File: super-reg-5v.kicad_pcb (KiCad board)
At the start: 2 copper layers, 80 x 34.3 mm, 40 parts, among them Q1 2SA1015, Q2 D44H11, U1 LM317T, U2 AD825, X1 AC_IN, X2 DC_OUT

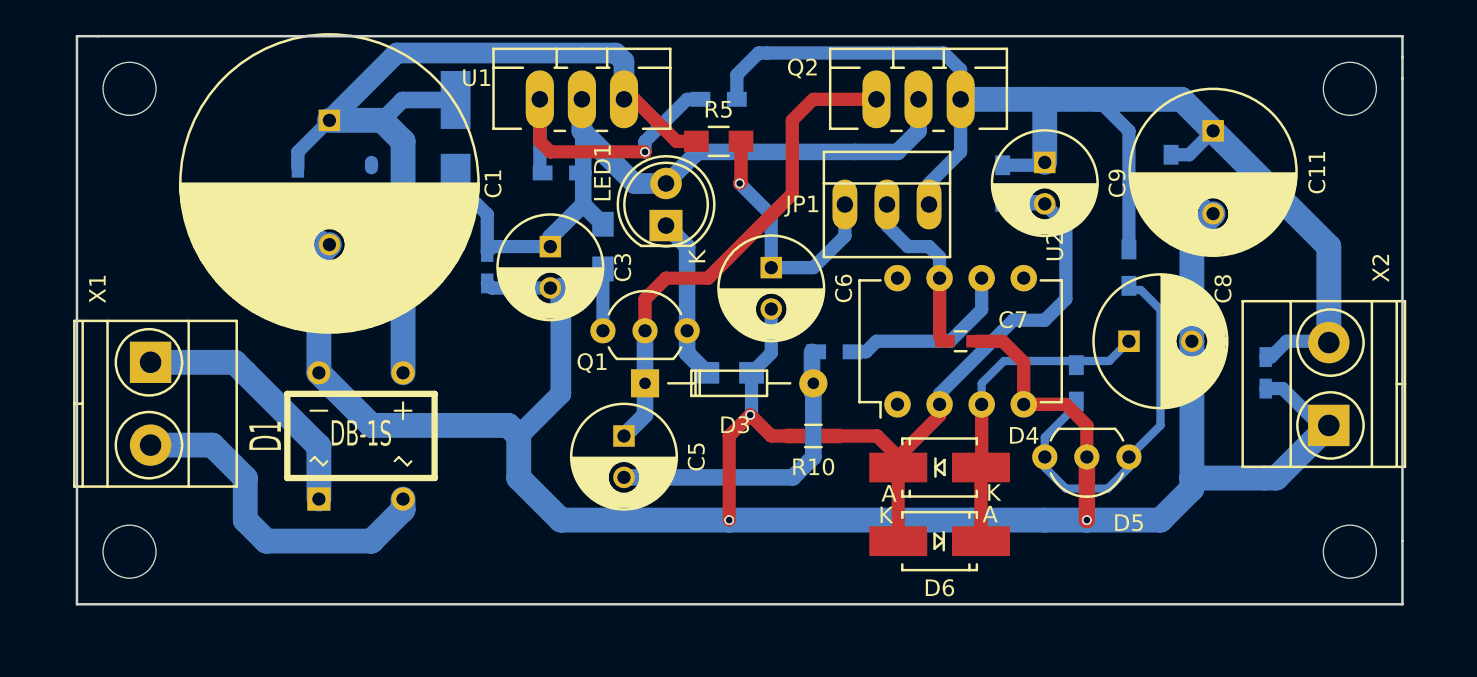
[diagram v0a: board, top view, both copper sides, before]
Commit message: change generic diode package to TUMD2 larger capacitor pad
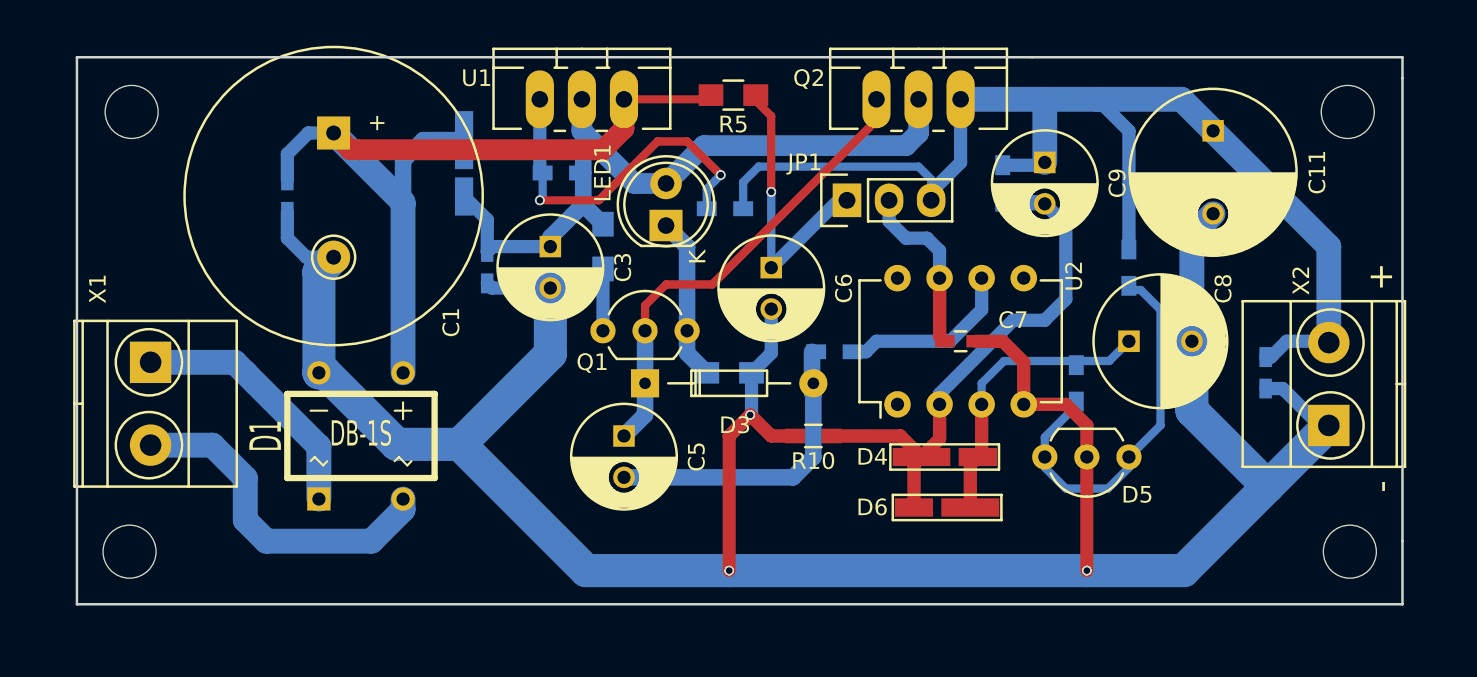
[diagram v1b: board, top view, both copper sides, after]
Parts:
- removed R11: 10k, Resistors_SMD:R_0603_HandSoldering
- C1: footprint Capacitors_ThroughHole:C_Radial_D18_L36_P7.5 -> myfootprint:C_Radial_D18_L36_P7.5_LargePad
- D2, D4, D6: footprint Diodes_SMD:SMA_Handsoldering -> myfootprint:TUMD2-handsoldering
- JP1: footprint Connect:PINHEAD1-3 -> Pin_Headers:Pin_Header_Straight_1x03
- moved R2 6.61 mm to (154.7, 82.8)
- moved R5 2.93 mm to (155.2, 75.9)
- moved JP1 2.43 mm to (162.1, 82.3), turned to 90 degrees
- moved D6 2.05 mm to (167.9, 100.8)
- moved D2 1.61 mm to (138.9, 80.3)
- moved ? 1.40 mm to (192.3, 77.0)
- moved REF** 1.40 mm to (118.9, 77.0)
- moved C2 0.99 mm to (128.3, 82.0)
- moved D4 0.81 mm to (168.1, 97.8)
- moved C1 0.80 mm to (131.1, 78.2)
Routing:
- net GND: track 150.7 -> 159.2 mm
- net Net-(C10-Pad1): track 79.5 -> 72.8 mm
- net Net-(R1-Pad2): track 19.0 -> 22.2 mm, vias 1 -> 2
- net Net-(C5-Pad1): track 30.4 -> 28.3 mm
- net Net-(C6-Pad1): track 15.6 -> 17.3 mm
- net Net-(C1-Pad1): track 54.9 -> 53.7 mm
- net Net-(C8-Pad1): track 18.8 -> 17.7 mm
- net Net-(C3-Pad1): track 45.2 -> 44.2 mm
- net Net-(C7-Pad1): track 10.4 -> 11.2 mm
- net (no net): track 0.52 -> 0.00 mm
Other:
- board size 80 x 34.3 mm -> 80 x 33 mm
- board text added: "+"
- board text added: "-"

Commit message: larger via pad size change silk for bridge-diode D1
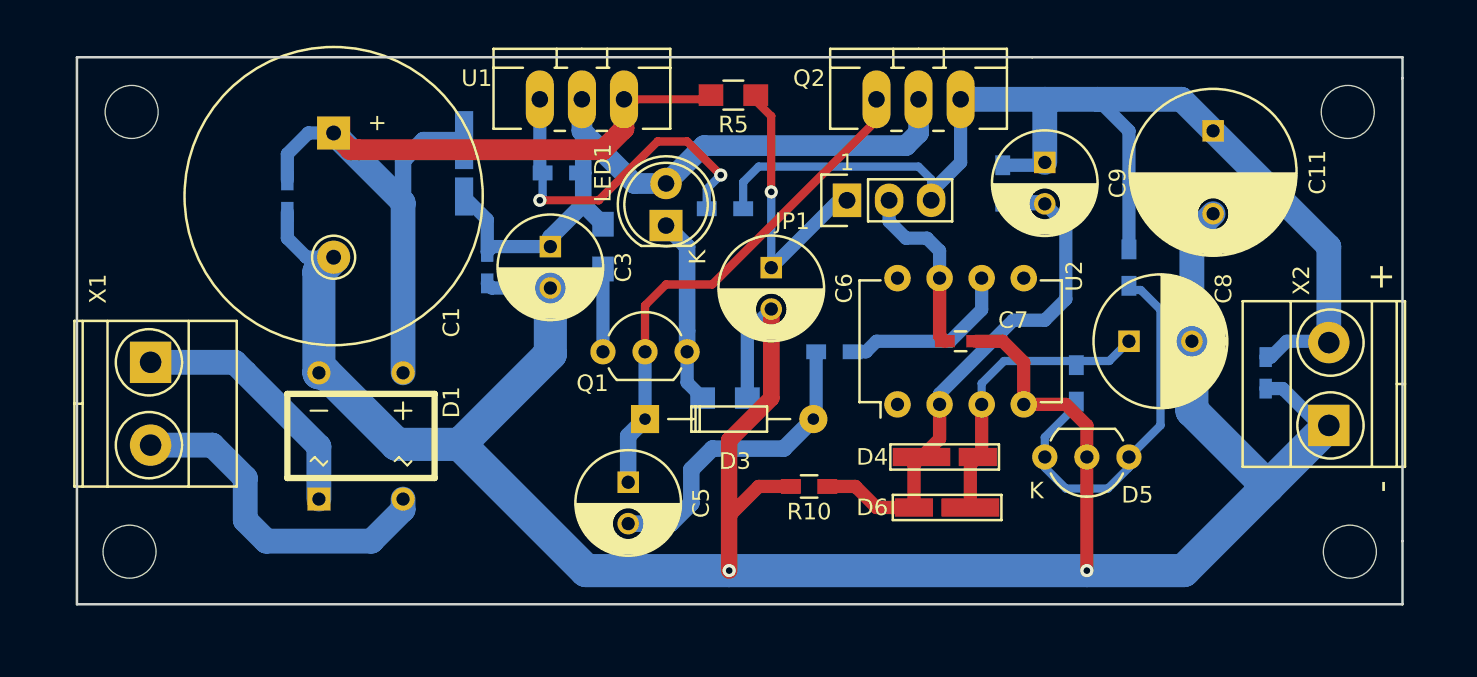
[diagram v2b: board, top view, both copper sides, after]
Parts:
- D1: footprint DB-1:D*** -> myfootprint:DB-1_DIP
- moved R10 3.06 mm to (159.8, 99.6)
- moved C5 2.81 mm to (148.8, 99.3)
- moved D3 2.16 mm to (149.9, 95.5)
- moved R3 1.55 mm to (154.7, 94.2)
- moved Q1 1.27 mm to (147.3, 91.4)
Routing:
- net GND: track 159.2 -> 169.9 mm, vias 3 -> 2
- net Net-(C5-Pad1): track 28.3 -> 31.0 mm
- net Net-(LED1-Pad1): track 9.91 -> 11.4 mm
- net Net-(Q1-Pad1): track 3.73 -> 5.00 mm
- net Net-(C5-Pad2): track 18.3 -> 19.1 mm
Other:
- net class Default: via_dia 0.6 -> 0.8
- board text added: "1"
- board text added: "K"

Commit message: minor track fix
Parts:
- moved ? 0.25 mm to (192.3, 77.2)
- moved REF** 0.25 mm to (118.9, 77.2)
- moved REF** 0.18 mm to (192.3, 103.4)
- moved REF** 0.18 mm to (118.9, 103.4)
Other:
- board size 80 x 33 mm -> 80 x 32.8 mm
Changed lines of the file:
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@@
     (links 63)
     (no_connects 0)
-    (area 106.014857 68.802 205.262143 110.245)
+    (area 106.014857 69.056 205.135143 110.118)
     (thickness 1.6)
-    (drawings 11)
+    (drawings 8)
     (tracks 199)
     (zones 0)
@@
   )
   (setup
-    (last_trace_width 0.8)
+    (last_trace_width 0.25)
     (user_trace_width 0.25)
     (user_trace_width 0.5)
@@
     (pad_to_mask_clearance 0.2)
     (aux_axis_origin 0 0)
+    (grid_origin 115.57 73.914)
     (visible_elements FFFFFF7F)
     (pcbplotparams
-      (layerselection 0x00030_80000001)
-      (usegerberextensions false)
+      (layerselection 0x010f0_80000001)
+      (usegerberextensions true)
       (excludeedgelayer true)
       (linewidth 0.100000)
@@
       (psa4output false)
       (plotreference true)
-      (plotvalue true)
+      (plotvalue false)
       (plotinvisibletext false)
       (padsonsilk false)
-      (subtractmaskfromsilk false)
+      (subtractmaskfromsilk true)
       (outputformat 1)
       (mirror false)
       (drillshape 0)
       (scaleselection 1)
-      (outputdirectory ""))
+      (outputdirectory gerber/))
   )
   (net 0 "")
@@
   )
   (module Mounting_Holes:MountingHole_3.2mm_M3 (layer F.Cu)
-    (at 118.745 103.505)
+    (at 118.872 103.378)
     (descr "Mounting Hole 3.2mm, no annular, M3")
     (tags "mounting hole 3.2mm no annular m3")
@@
   )
   (module Mounting_Holes:MountingHole_3.2mm_M3 (layer F.Cu)
-    (at 192.405 103.505)
+    (at 192.278 103.378)
     (descr "Mounting Hole 3.2mm, no annular, M3")
     (tags "mounting hole 3.2mm no annular m3")
@@
   )
   (module Mounting_Holes:MountingHole_3.2mm_M3 (layer F.Cu)
-    (at 118.872 76.962)
+    (at 118.872 77.216)
     (descr "Mounting Hole 3.2mm, no annular, M3")
     (tags "mounting hole 3.2mm no annular m3")
@@
   )
   (module Mounting_Holes:MountingHole_3.2mm_M3 (layer F.Cu)
-    (at 192.278 76.962)
+    (at 192.278 77.216)
     (descr "Mounting Hole 3.2mm, no annular, M3")
     (tags "mounting hole 3.2mm no annular m3")
@@
     )
   )
+  (gr_line (start 195.58 73.914) (end 195.58 106.68) (angle 90) (layer Edge.Cuts) (width 0.15))
+  (gr_line (start 115.57 73.914) (end 115.57 106.68) (angle 90) (layer Edge.Cuts) (width 0.15))
+  (gr_line (start 195.58 73.914) (end 115.57 73.914) (angle 90) (layer Edge.Cuts) (width 0.15))
   (gr_text 1 (at 162.052 80.01) (layer F.SilkS)
     (effects (font (size 1 1) (thickness 0.15)))
@@
     (effects (font (size 1 1) (thickness 0.15)))
   )
-  (gr_line (start 173.228 73.66) (end 195.58 73.66) (angle 90) (layer Edge.Cuts) (width 0.15))
-  (gr_line (start 115.57 106.68) (end 115.57 73.66) (angle 90) (layer Edge.Cuts) (width 0.15))
-  (gr_line (start 173.228 73.66) (end 115.57 73.66) (angle 90) (layer Edge.Cuts) (width 0.15))
   (gr_text - (at 194.31 99.568 90) (layer F.SilkS)
     (effects (font (size 1.5 1.5) (thickness 0.3)))
@@
     (effects (font (size 1.5 1.5) (thickness 0.3)))
   )
-  (gr_line (start 195.58 106.68) (end 195.58 102.87) (angle 90) (layer Edge.Cuts) (width 0.15))
   (gr_line (start 115.57 106.68) (end 195.58 106.68) (angle 90) (layer Edge.Cuts) (width 0.15))
-  (gr_line (start 195.58 74.93) (end 195.58 73.66) (angle 90) (layer Edge.Cuts) (width 0.15))
-  (gr_line (start 195.58 102.87) (end 195.58 74.93) (angle 90) (layer Edge.Cuts) (width 0.15))
   (segment (start 135.255 82.55) (end 135.255 79.883) (width 1) (layer B.Cu) (net 1))
   (segment (start 136.474 78.664) (end 138.938 78.664) (width 1) (layer B.Cu) (net 1))
@@
   (segment (start 153.59 76.2) (end 153.844 75.946) (width 0.5) (layer F.Cu) (net 1))
   (segment (start 138.862 78.74) (end 138.938 78.664) (width 0.8) (layer B.Cu) (net 1))
-  (segment (start 156.036 94.234) (end 156.036 90.304) (width 0.8) (layer B.Cu) (net 2) (status 400000))
-  (segment (start 156.036 90.304) (end 157.48 88.86) (width 0.8) (layer B.Cu) (net 2) (status 800000))
+  (segment (start 156.036 94.234) (end 156.036 90.304) (width 0.8) (layer B.Cu) (net 2))
+  (segment (start 156.036 90.304) (end 157.48 88.86) (width 0.8) (layer B.Cu) (net 2))
   (segment (start 154.94 104.648) (end 154.94 96.774) (width 1) (layer F.Cu) (net 2))
-  (segment (start 157.48 94.234) (end 157.48 88.86) (width 1) (layer F.Cu) (net 2) (status 800000))
+  (segment (start 157.48 94.234) (end 157.48 88.86) (width 1) (layer F.Cu) (net 2))
   (segment (start 154.94 96.774) (end 157.48 94.234) (width 1) (layer F.Cu) (net 2))
   (segment (start 158.666 99.568) (end 156.718 99.568) (width 0.8) (layer F.Cu) (net 2))
@@
   (segment (start 154.94 101.346) (end 154.94 104.648) (width 0.8) (layer F.Cu) (net 2))
   (segment (start 176.53 97.79) (end 176.53 104.648) (width 0.8) (layer F.Cu) (net 2))
-  (via (at 176.53 104.648) (size 0.8) (drill 0.4) (layers F.Cu B.Cu) (net 2) (status 1000000))
+  (via (at 176.53 104.648) (size 0.8) (drill 0.4) (layers F.Cu B.Cu) (net 2))
   (segment (start 182.87 90.805) (end 182.87 94.986) (width 2) (layer B.Cu) (net 2))
   (segment (start 182.87 94.986) (end 187.452 99.568) (width 2) (layer B.Cu) (net 2))
@@
   (segment (start 170.18 93.345) (end 171.53 91.995) (width 0.5) (layer B.Cu) (net 7))
   (segment (start 171.53 91.995) (end 175.895 91.995) (width 0.5) (layer B.Cu) (net 7))
-  (segment (start 155.786 82.804) (end 155.786 81.196) (width 0.5) (layer B.Cu) (net 8))
-  (segment (start 167.132 81.026) (end 167.132 82.296) (width 0.5) (layer B.Cu) (net 8))
-  (segment (start 166.37 80.264) (end 167.132 81.026) (width 0.5) (layer B.Cu) (net 8))
-  (segment (start 156.718 80.264) (end 166.37 80.264) (width 0.5) (layer B.Cu) (net 8))
-  (segment (start 155.786 81.196) (end 156.718 80.264) (width 0.5) (layer B.Cu) (net 8))
+  (segment (start 167.132 82.296) (end 167.132 81.28) (width 0.5) (layer B.Cu) (net 8))
+  (segment (start 167.132 81.28) (end 166.37 80.518) (width 0.5) (layer B.Cu) (net 8))
+  (segment (start 166.37 80.518) (end 156.464 80.518) (width 0.5) (layer B.Cu) (net 8))
+  (segment (start 156.464 80.518) (end 155.786 81.196) (width 0.5) (layer B.Cu) (net 8))
+  (segment (start 155.786 81.196) (end 155.786 82.804) (width 0.5) (layer B.Cu) (net 8))
   (segment (start 168.91 76.2) (end 168.91 80.01) (width 0.8) (layer B.Cu) (net 8))
   (segment (start 168.91 80.01) (end 167.132 81.788) (width 0.8) (layer B.Cu) (net 8))

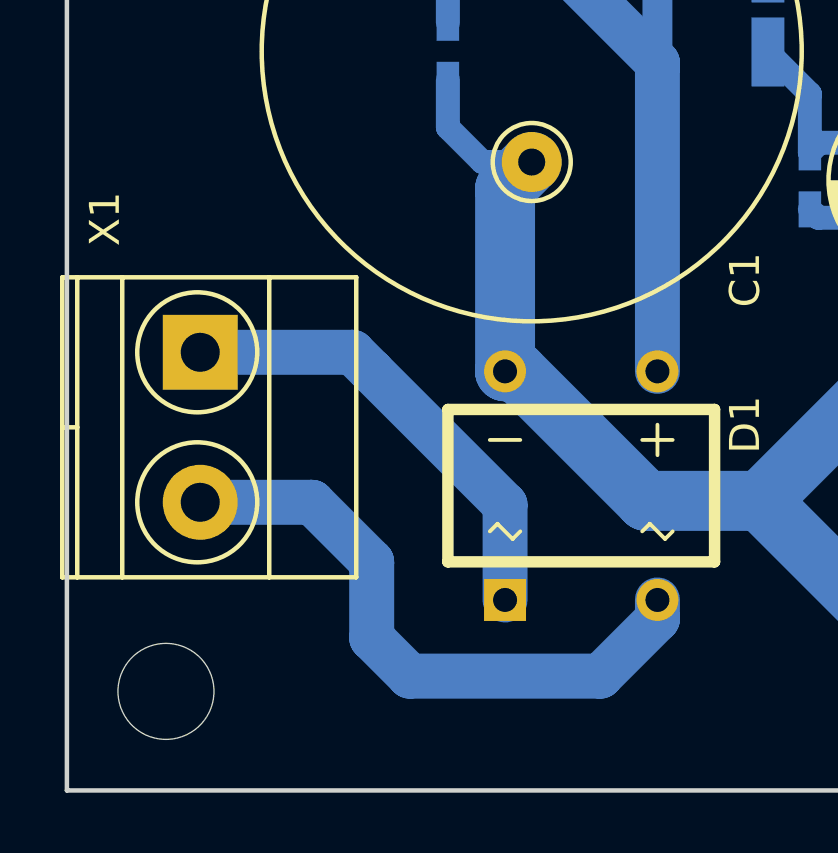
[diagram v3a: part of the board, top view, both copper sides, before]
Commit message: Add AC silk and dates
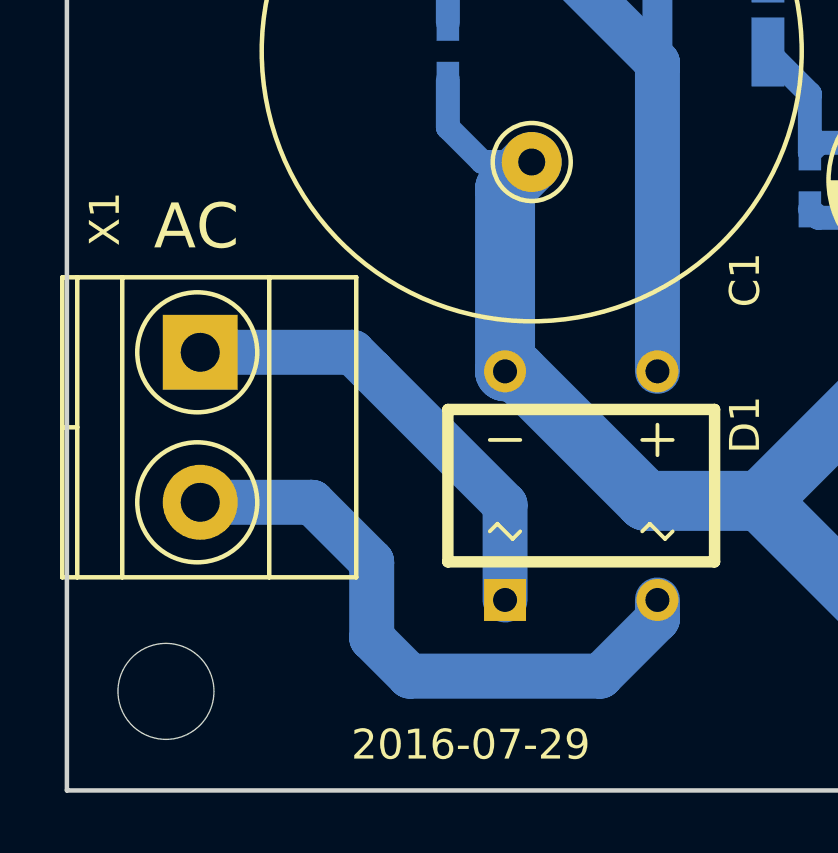
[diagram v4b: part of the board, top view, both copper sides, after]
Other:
- board text added: "2016-07-29"
- board text added: "AC"
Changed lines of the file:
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@@
     (area 106.014857 69.056 205.135143 110.118)
     (thickness 1.6)
-    (drawings 8)
+    (drawings 10)
     (tracks 199)
     (zones 0)
@@
     )
   )
+  (gr_text 2016-07-29 (at 129.032 105.156) (layer F.SilkS)
+    (effects (font (size 1 1) (thickness 0.25)))
+  )
+  (gr_text AC (at 119.888 87.884) (layer F.SilkS)
+    (effects (font (size 1.5 1.5) (thickness 0.3)))
+  )
   (gr_line (start 195.58 73.914) (end 195.58 106.68) (angle 90) (layer Edge.Cuts) (width 0.15))
